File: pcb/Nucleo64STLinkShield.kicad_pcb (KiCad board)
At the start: 4 copper layers, 0 parts

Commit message: Imported debug connector from design block.
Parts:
- added J1: Debug, pcb:Molex_PicoBlade_53047-1010_1x10_P1.25mm_Vertical, F.Cu at (148.2, 102.0)

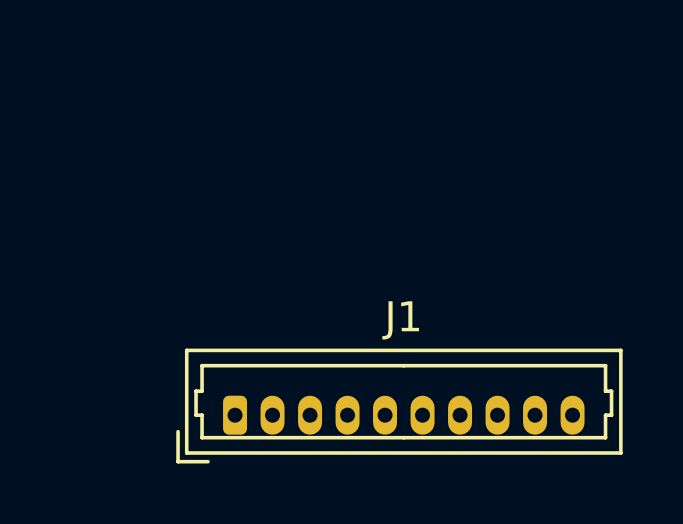
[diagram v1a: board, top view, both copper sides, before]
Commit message: Imported Nucleo-64 ST-Link debugger model.
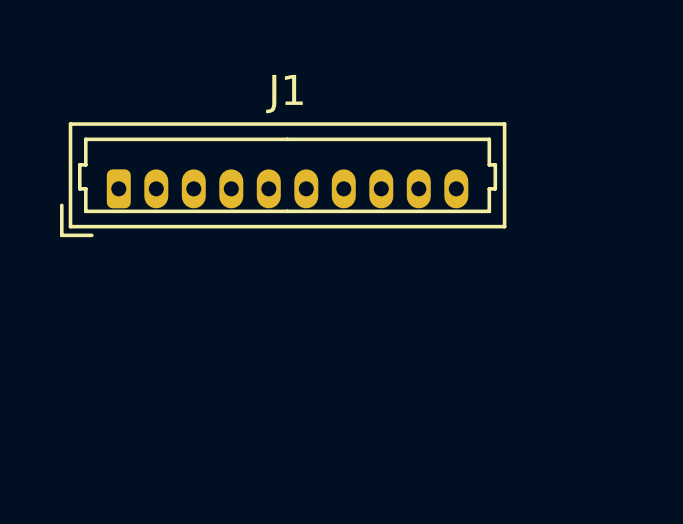
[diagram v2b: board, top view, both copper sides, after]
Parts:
- added N1: Housing, pcb:Nucleo64STLinkShieldHousing, F.Cu at (150.0, 100.0)
- moved J1 8.48 mm to (144.4, 94.5)
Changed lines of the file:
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@@
 	(net 7 "SWDIO")
 	(net 8 "SWO")
+	(footprint "pcb:Nucleo64STLinkShieldHousing"
+		(locked yes)
+		(layer "F.Cu")
+		(at 150 100)
+		(descr "Housing for the Main Camera System.")
+		(property "Reference" "N1"
+			(at 0 -0.5 0)
+			(unlocked yes)
+			(layer "F.SilkS")
+			(hide yes)
+			(effects
+				(font
+					(size 1 1)
+					(thickness 0.1)
+				)
+			)
+		)
+		(property "Value" "Housing"
+			(at 0 1 0)
+			(unlocked yes)
+			(layer "F.Fab")
+			(hide yes)
+			(effects
+				(font
+					(size 1 1)
+					(thickness 0.15)
+				)
+			)
+		)
+		(property "Datasheet" "~"
+			(at 0 0 0)
+			(unlocked yes)
+			(layer "F.Fab")
+			(hide yes)
+			(effects
+				(font
+					(size 1 1)
+					(thickness 0.15)
+				)
+			)
+		)
+		(property "Description" "Housing"
+			(at 0 0 0)
+			(unlocked yes)
+			(layer "F.Fab")
+			(hide yes)
+			(effects
+				(font
+					(size 1 1)
+					(thickness 0.15)
+				)
+			)
+		)
+		(property ki_fp_filters "Enclosure* Housing*")
+		(sheetname "/")
+		(sheetfile "Nucleo64STLinkShield.kicad_sch")
+		(attr smd)
+		(fp_line
+			(start -1 0)
+			(end 1 0)
+			(stroke
+				(width 0.1)
+				(type default)
+			)
+			(layer "User.1")
+		)
+		(fp_line
+			(start 0 -1)
+			(end 0 1)
+			(stroke
+				(width 0.1)
+				(type default)
+			)
+			(layer "User.1")
+		)
+		(fp_circle
+			(center 0 0)
+			(end 1 0)
+			(stroke
+				(width 0.1)
+				(type default)
+			)
+			(fill no)
+			(layer "User.1")
+		)
+		(embedded_fonts no)
+		(model "${KIPRJMOD}/models/Nucleo64_STLink_Debugger.step"
+			(offset
+				(xyz 10 -31.5 -12.8)
+			)
+			(scale
+				(xyz 1 1 1)
+			)
+			(rotate
+				(xyz -90 -0 -0)
+			)
+		)
+	)
 	(footprint "pcb:Molex_PicoBlade_53047-1010_1x10_P1.25mm_Vertical"
 		(layer "F.Cu")
-		(at 148.25 102)
+		(at 144.375 94.455)
 		(descr "Molex PicoBlade Connector System, 53047-1010, 10 Pins per row (http://www.molex.com/pdm_docs/sd/530470610_sd.pdf), generated with kicad-footprint-generator")
 		(tags "connector Molex PicoBlade vertical")

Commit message: Updated debug connector symbol from 02x05 to 01x10.
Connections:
- J1 pad 2: GND -> RESET
- J1 pad 3: RESET -> STLINK_TX
- J1 pad 4: SWCLK -> STLINK_RX
- J1 pad 5: STLINK_TX -> GND
- J1 pad 6: SWDIO -> GND
- J1 pad 7: STLINK_RX -> SWCLK
- J1 pad 8: SWO -> SWDIO
- J1 pad 9: GND -> SWO
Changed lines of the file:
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@@
 			)
 		)
-		(property "Description" "Generic connector, double row, 02x05, odd/even pin numbering scheme (row 1 odd numbers, row 2 even numbers), script generated (kicad-library-utils/schlib/autogen/connector/)"
+		(property "Description" "Generic connector, single row, 01x10, script generated (kicad-library-utils/schlib/autogen/connector/)"
 			(at 0 0 0)
 			(layer "F.Fab")
@@
 			)
 		)
-		(property ki_fp_filters "Connector*:*_2x??_*")
+		(property ki_fp_filters "Connector*:*_1x??_*")
 		(sheetname "/")
 		(sheetfile "Nucleo64STLinkShield.kicad_sch")
@@
 			(layers "*.Cu" "*.Mask")
 			(remove_unused_layers no)
-			(net 1 "GND")
+			(net 5 "RESET")
 			(pinfunction "Pin_2")
 			(pintype "passive")
@@
 			(layers "*.Cu" "*.Mask")
 			(remove_unused_layers no)
-			(net 5 "RESET")
+			(net 2 "STLINK_TX")
 			(pinfunction "Pin_3")
 			(pintype "passive")
@@
 			(layers "*.Cu" "*.Mask")
 			(remove_unused_layers no)
-			(net 4 "SWCLK")
+			(net 6 "STLINK_RX")
 			(pinfunction "Pin_4")
 			(pintype "passive")
@@
 			(layers "*.Cu" "*.Mask")
 			(remove_unused_layers no)
-			(net 2 "STLINK_TX")
+			(net 1 "GND")
 			(pinfunction "Pin_5")
 			(pintype "passive")
@@
 			(layers "*.Cu" "*.Mask")
 			(remove_unused_layers no)
-			(net 7 "SWDIO")
+			(net 1 "GND")
 			(pinfunction "Pin_6")
 			(pintype "passive")
@@
 			(layers "*.Cu" "*.Mask")
 			(remove_unused_layers no)
-			(net 6 "STLINK_RX")
+			(net 4 "SWCLK")
 			(pinfunction "Pin_7")
 			(pintype "passive")
@@
 			(layers "*.Cu" "*.Mask")
 			(remove_unused_layers no)
-			(net 8 "SWO")
+			(net 7 "SWDIO")
 			(pinfunction "Pin_8")
 			(pintype "passive")
@@
 			(layers "*.Cu" "*.Mask")
 			(remove_unused_layers no)
-			(net 1 "GND")
+			(net 8 "SWO")
 			(pinfunction "Pin_9")
 			(pintype "passive")

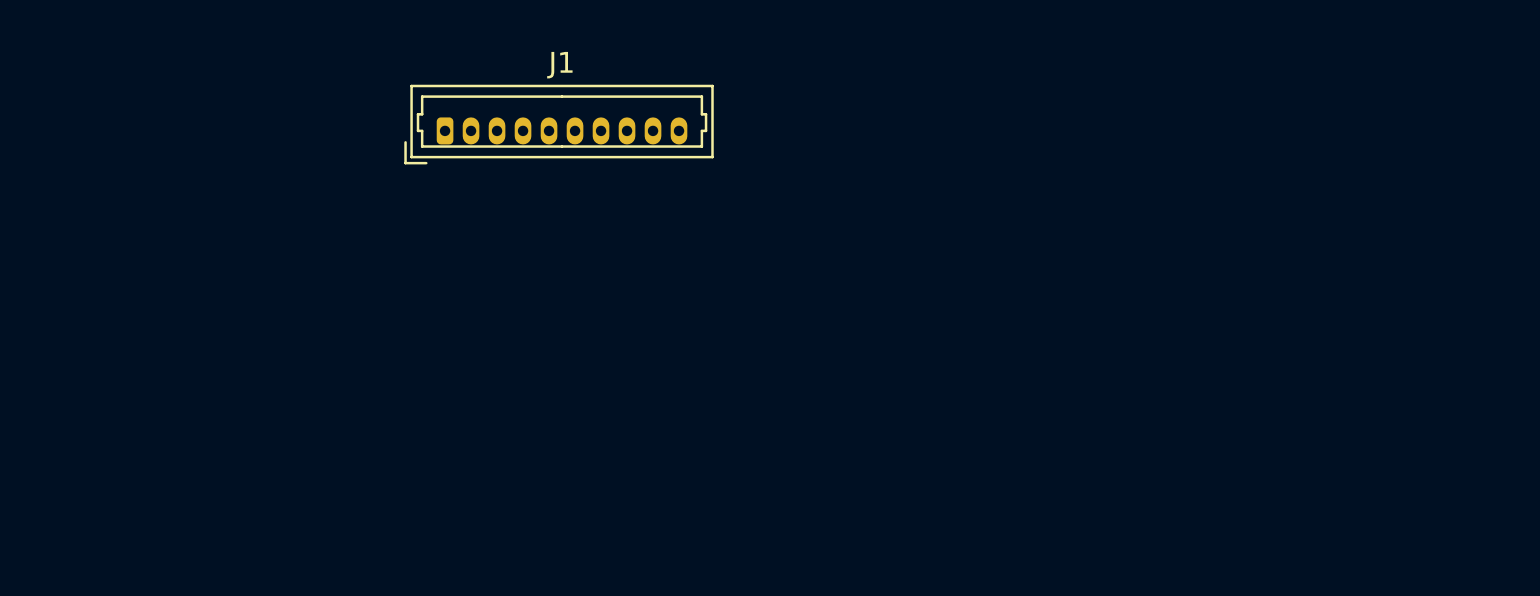
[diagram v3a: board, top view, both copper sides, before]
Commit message: Made edge cuts.
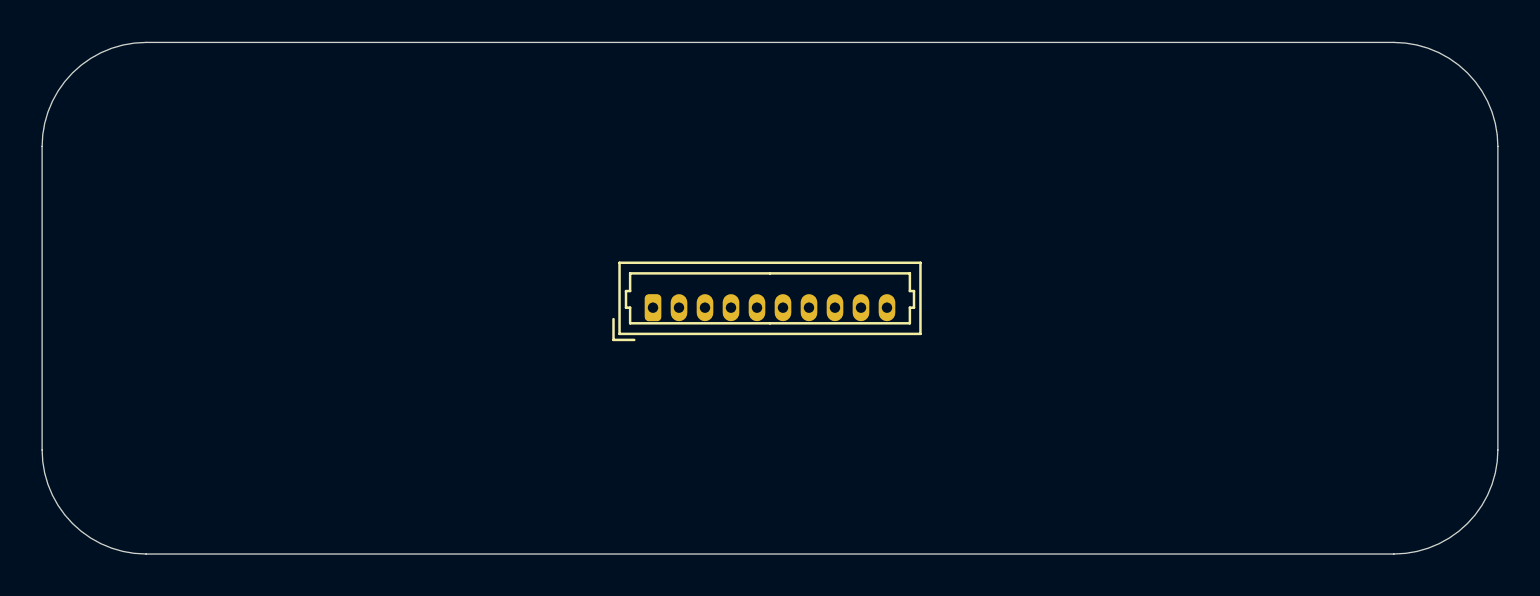
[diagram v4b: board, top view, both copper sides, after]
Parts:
- removed J1: Debug, pcb:Molex_PicoBlade_53047-1010_1x10_P1.25mm_Vertical
- added J2: Debug, pcb:Molex_PicoBlade_53047-1010_1x10_P1.25mm_Vertical, F.Cu at (154.4, 103.0)
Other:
- board outline added: 70 x 24.6 mm
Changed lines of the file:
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@@
 	(net 0 "")
 	(net 1 "GND")
-	(net 2 "STLINK_TX")
-	(net 3 "+3.3V")
-	(net 4 "SWCLK")
-	(net 5 "RESET")
-	(net 6 "STLINK_RX")
-	(net 7 "SWDIO")
-	(net 8 "SWO")
+	(net 2 "+3.3V")
+	(net 3 "RESET")
+	(net 4 "swdio")
+	(net 5 "swclk")
+	(net 6 "stlink_tx")
+	(net 7 "swo")
+	(net 8 "stlink_rx")
 	(footprint "pcb:Nucleo64STLinkShieldHousing"
 		(locked yes)
@@
 	)
 	(footprint "pcb:Molex_PicoBlade_53047-1010_1x10_P1.25mm_Vertical"
+		(locked yes)
 		(layer "F.Cu")
-		(at 144.375 94.455)
+		(at 154.375 102.955)
 		(descr "Molex PicoBlade Connector System, 53047-1010, 10 Pins per row (http://www.molex.com/pdm_docs/sd/530470610_sd.pdf), generated with kicad-footprint-generator")
 		(tags "connector Molex PicoBlade vertical")
-		(property "Reference" "J1"
+		(property "Reference" "J2"
 			(at 5.62 -3.26 0)
 			(layer "F.SilkS")
+			(hide yes)
 			(effects
 				(font
@@
 			(remove_unused_layers no)
 			(roundrect_rratio 0.25)
-			(net 3 "+3.3V")
+			(net 2 "+3.3V")
 			(pinfunction "Pin_1")
 			(pintype "passive")
@@
 			(layers "*.Cu" "*.Mask")
 			(remove_unused_layers no)
-			(net 5 "RESET")
+			(net 3 "RESET")
 			(pinfunction "Pin_2")
 			(pintype "passive")
@@
 			(layers "*.Cu" "*.Mask")
 			(remove_unused_layers no)
-			(net 2 "STLINK_TX")
+			(net 6 "stlink_tx")
 			(pinfunction "Pin_3")
 			(pintype "passive")
@@
 			(layers "*.Cu" "*.Mask")
 			(remove_unused_layers no)
-			(net 6 "STLINK_RX")
+			(net 8 "stlink_rx")
 			(pinfunction "Pin_4")
 			(pintype "passive")
@@
 			(layers "*.Cu" "*.Mask")
 			(remove_unused_layers no)
-			(net 4 "SWCLK")
+			(net 5 "swclk")
 			(pinfunction "Pin_7")
 			(pintype "passive")
@@
 			(layers "*.Cu" "*.Mask")
 			(remove_unused_layers no)
-			(net 7 "SWDIO")
+			(net 4 "swdio")
 			(pinfunction "Pin_8")
 			(pintype "passive")
@@
 			(layers "*.Cu" "*.Mask")
 			(remove_unused_layers no)
-			(net 8 "SWO")
+			(net 7 "swo")
 			(pinfunction "Pin_9")
 			(pintype "passive")
@@
 		)
 	)
+	(gr_arc
+		(start 125 95.2)
+		(mid 126.464466 91.664466)
+		(end 130 90.2)
+		(stroke
+			(width 0.05)
+			(type default)
+		)
+		(locked yes)
+		(layer "Edge.Cuts")
+	)
+	(gr_line
+		(start 190 114.8)
+		(end 130 114.8)
+		(stroke
+			(width 0.05)
+			(type default)
+		)
+		(locked yes)
+		(layer "Edge.Cuts")
+	)
+	(gr_line
+		(start 195 95.2)
+		(end 195 109.8)
+		(stroke
+			(width 0.05)
+			(type default)
+		)
+		(locked yes)
+		(layer "Edge.Cuts")
+	)
+	(gr_arc
+		(start 190 90.2)
+		(mid 193.535534 91.664466)
+		(end 195 95.2)
+		(stroke
+			(width 0.05)
+			(type default)
+		)
+		(locked yes)
+		(layer "Edge.Cuts")
+	)
+	(gr_arc
+		(start 130 114.8)
+		(mid 126.464466 113.335534)
+		(end 125 109.8)
+		(stroke
+			(width 0.05)
+			(type default)
+		)
+		(locked yes)
+		(layer "Edge.Cuts")
+	)
+	(gr_line
+		(start 125 109.8)
+		(end 125 95.2)
+		(stroke
+			(width 0.05)
+			(type default)
+		)
+		(locked yes)
+		(layer "Edge.Cuts")
+	)
+	(gr_line
+		(start 130 90.2)
+		(end 190 90.2)
+		(stroke
+			(width 0.05)
+			(type default)
+		)
+		(locked yes)
+		(layer "Edge.Cuts")
+	)
+	(gr_arc
+		(start 195 109.8)
+		(mid 193.535534 113.335534)
+		(end 190 114.8)
+		(stroke
+			(width 0.05)
+			(type default)
+		)
+		(locked yes)
+		(layer "Edge.Cuts")
+	)
 	(embedded_fonts no)

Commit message: Added 2.54mm pin sockets to ST-Link.
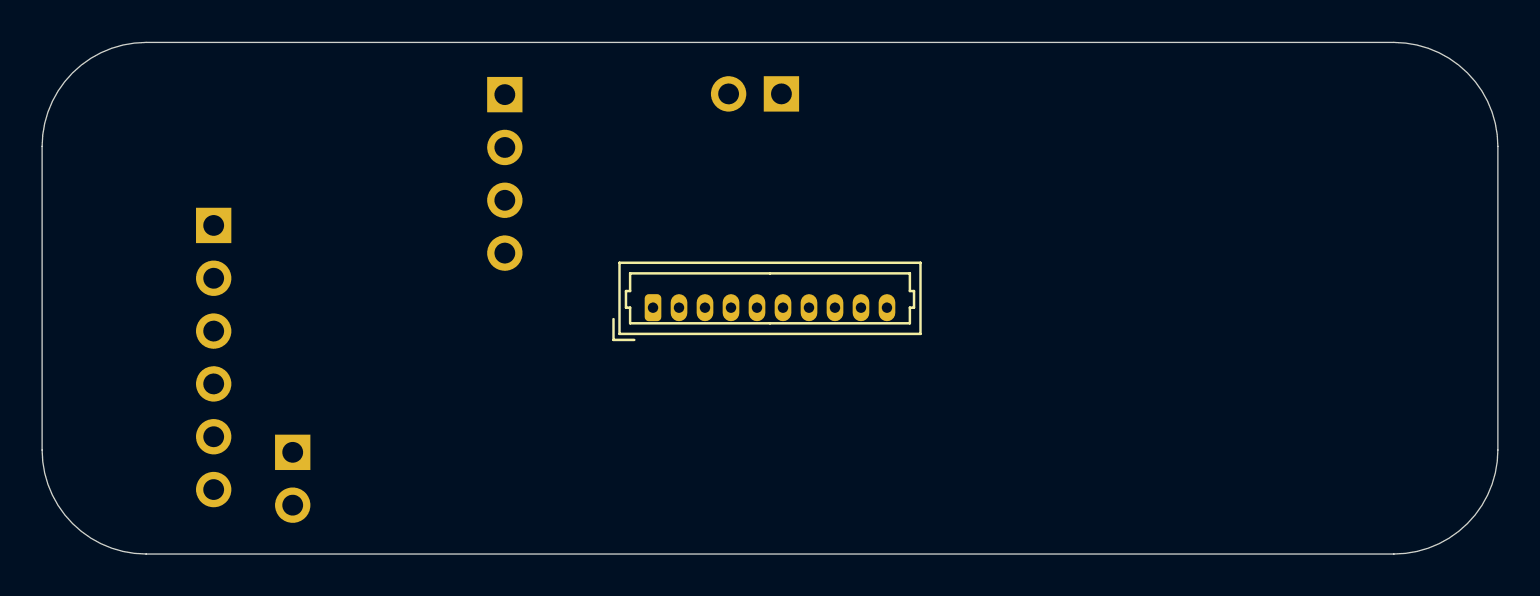
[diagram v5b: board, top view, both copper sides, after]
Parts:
- added J1: SWD, Connector_PinSocket_2.54mm:PinSocket_1x06_P2.54mm_Vertical, B.Cu at (133.2, 99.0)
- added J3: UART, Connector_PinSocket_2.54mm:PinSocket_1x02_P2.54mm_Vertical, B.Cu at (137.1, 109.9)
- added J4: USB Power, Connector_PinSocket_2.54mm:PinSocket_1x02_P2.54mm_Vertical, B.Cu at (160.6, 92.7)
- added J5: Nucleo-64 ST-Link Selector, Connector_PinSocket_2.54mm:PinSocket_1x04_P2.54mm_Vertical, B.Cu at (147.2, 92.7)

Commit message: Added QR code and shrunk edge-cut.
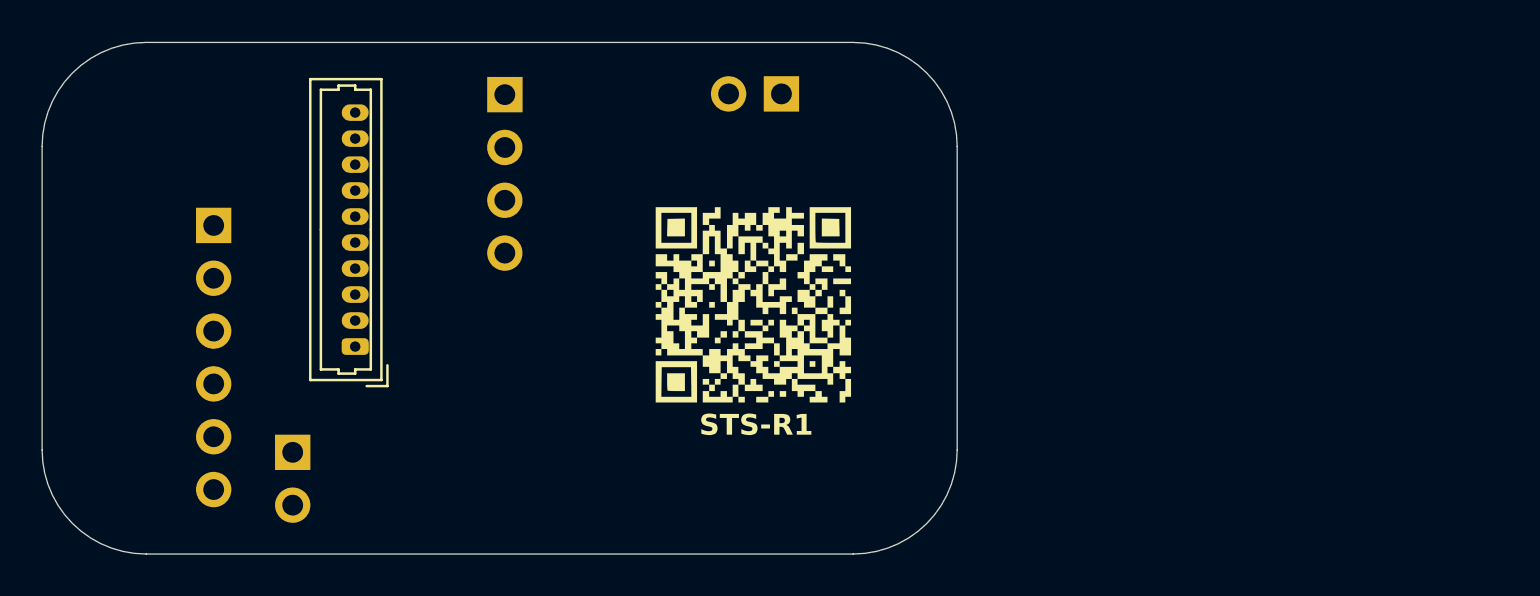
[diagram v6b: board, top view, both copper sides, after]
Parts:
- added G***: LOGO, LOGO, F.Cu at (159.2, 102.8)
- moved J2 14.4 mm to (140.1, 104.8), turned to 90 degrees
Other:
- board size 70 x 24.6 mm -> 44 x 24.6 mm
- board text added: "STS-R1"
